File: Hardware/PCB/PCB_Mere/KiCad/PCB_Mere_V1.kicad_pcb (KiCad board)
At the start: 4 copper layers, 73 parts, among them CN1 FTSH-107-01-L-DV-K-A, CN2 B4B-PH-K-S_GNSS, SW1 NRST_BTN, SW2 BOOT_BTN, U1 STM32H723ZGT6, U2 LORA1276-C1-868MHZ, U3 ESP32C3-SUPERMINI, U4 BNO055, U5 B8B-PH-K-S-_TACTIL, U6 B8B-PH-K-S_FILS, U7 B10B-PH-K-S-_SCRN/JOY/ALIM, U8 A-SP1102AR6GHC-A01-2C

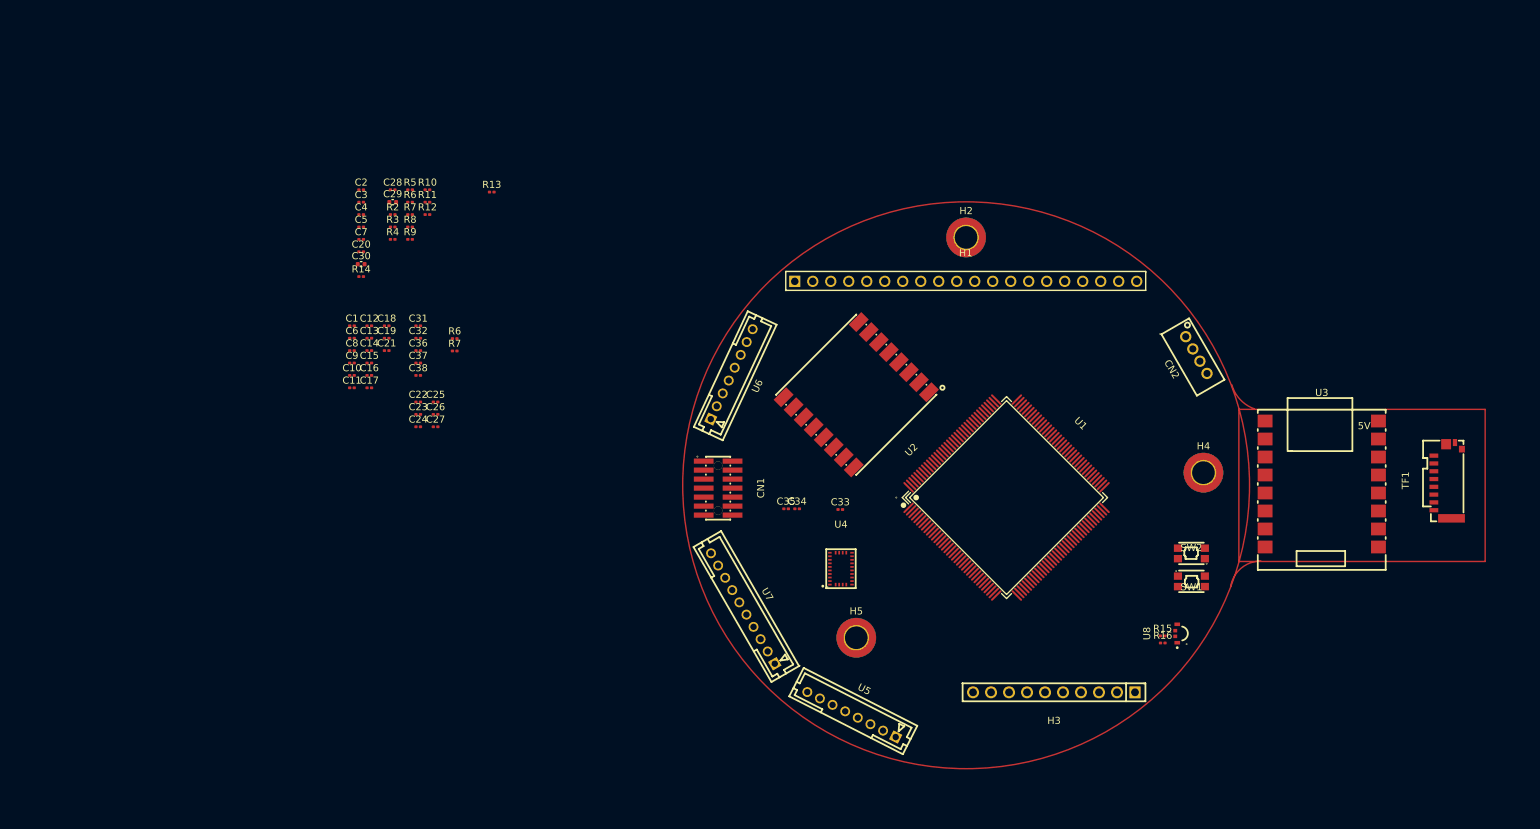
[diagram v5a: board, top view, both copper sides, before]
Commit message: Push PCB_Mère avancement routage
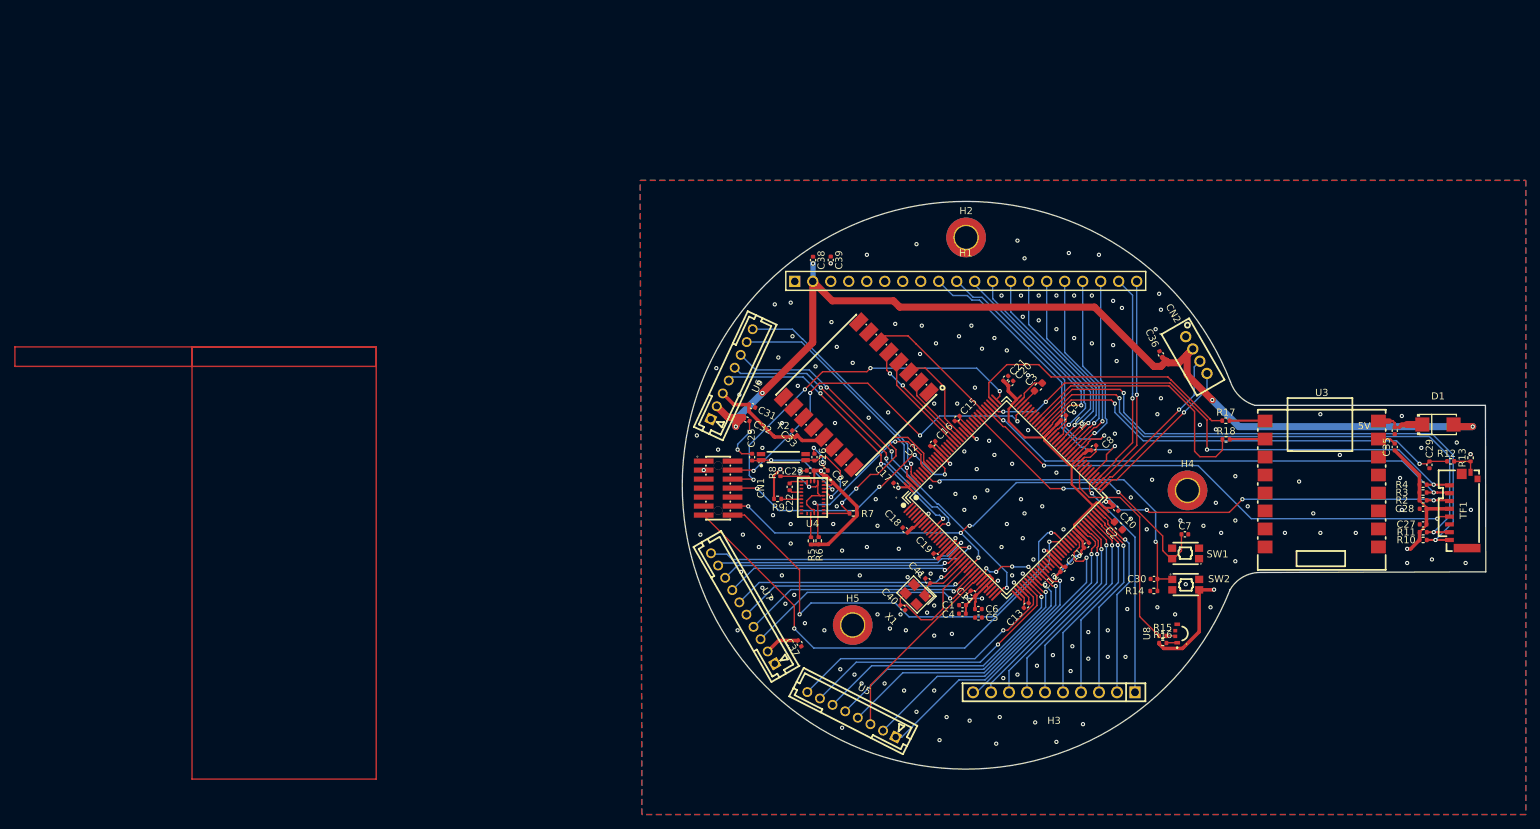
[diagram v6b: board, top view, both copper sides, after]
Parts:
- removed the R6 at (92.0, 53.3)
- removed the R7 at (92.0, 55.1)
- added C39: 100n, Capacitor_SMD:C_0402_1005Metric, F.Cu at (151.4, 61.5)
- added C40: 22p, Capacitor_SMD:C_0402_1005Metric, F.Cu at (161.6, 110.5)
- added C41: 22p, Capacitor_SMD:C_0402_1005Metric, F.Cu at (165.1, 106.8)
- added D1: SS34_C8678, EasyEDA:SMA_L4.3-W2.6-LS5.2-RD, F.Cu at (237.1, 84.7)
- added R17: 1k, Resistor_SMD:R_0402_1005Metric, F.Cu at (207.2, 84.2)
- added R18: 1k, Resistor_SMD:R_0402_1005Metric, F.Cu at (207.2, 86.8)
- added X1: X322525MOB4SI, EasyEDA:CRYSTAL-SMD_4P-L3.2-W2.5-BL, F.Cu at (163.3, 108.7)
- added X2: X701532768KGD4GI, EasyEDA:MC-146_4P-L6.7-W1.5-P0.85-BL, F.Cu at (144.7, 89.3)
- C1, C10, C11, C12, C13, C14, C15, C16, C17, C18, C19, C20, C21, C22, C24, C25, C26, C27, C28, C31, C32, C33, C34, C35, C36, C37, C38, C4, C5, C6, C7, C8, C9: footprint Capacitor_SMD:C_0201_0603Metric -> Capacitor_SMD:C_0402_1005Metric
- C2, C3: footprint Capacitor_SMD:C_0201_0603Metric -> Capacitor_SMD:C_0603_1608Metric
- C23: value 120n -> 100n; footprint Capacitor_SMD:C_0201_0603Metric -> Capacitor_SMD:C_0402_1005Metric
- R10, R11, R12, R13, R14, R15, R16, R2, R3, R4, R5, R6, R7, R8, R9: footprint Resistor_SMD:R_0201_0603Metric -> Resistor_SMD:R_0402_1005Metric
- moved C28 152.2 mm to (235.0, 96.6)
- moved C29 150.9 mm to (235.9, 90.4), turned to -90 degrees
- moved R2 150.9 mm to (235.0, 95.4)
- moved R3 150.2 mm to (235.0, 94.3)
- moved R4 149.5 mm to (235.0, 93.2)
- moved R10 149.0 mm to (235.0, 101.0)
- moved R12 148.6 mm to (238.9, 89.9)
- moved R11 148.1 mm to (235.0, 99.9)
- moved R13 143.1 mm to (241.7, 89.4), turned to 90 degrees
- moved C27 140.1 mm to (235.0, 98.8), turned to 180 degrees
- moved C7 123.5 mm to (201.4, 100.2)
- moved C30 120.4 mm to (197.0, 106.5)
- moved R14 120.4 mm to (197.0, 108.2), turned to 180 degrees
- moved C2 116.9 mm to (192.0, 99.0), turned to 135 degrees
- moved C10 109.4 mm to (191.6, 96.5), turned to -45 degrees
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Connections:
- net TMC2209_AZ_STEP_GPIO_Output renamed TMC2209_AZ_SPREAD_GPIO_Output
- net TMC2209_EL_STEP_GPIO_Output renamed TMC2209_EL_SPREAD_GPIO_Output
- C34 pad 2: +5V -> Net-(D1-K)
- H1 pad 10: unconnected-(H1-Pad10) -> TMC2209_AZ_STDBY_GPIO_Output
- H1 pad 3: unconnected-(H1-Pad3) -> +3.3V
- H1 pad 9: unconnected-(H1-Pad9) -> TMC2209_EL_STDBY_GPIO_Output
- U1 pad 100: unconnected-(U1-PA8-Pad100) -> Net-(U1-PA8)
- U1 pad 110: unconnected-(U1-PA15-Pad110) -> Net-(U1-PA15)
- U1 pad 114: unconnected-(U1-PD0-Pad114) -> LoRa_NRST_STM_GPIO_Output
- U1 pad 23: unconnected-(U1-PH0-OSC_IN-Pad23) -> /OSC_IN
- U1 pad 24: unconnected-(U1-PH1-OSC_OUT-Pad24) -> /OSC_OUT
- U1 pad 58: ESP32_UART7_RX -> unconnected-(U1-PE7-Pad58)
- U1 pad 59: ESP32_UART7_TX -> unconnected-(U1-PE8-Pad59)
- U1 pad 78: unconnected-(U1-PD9-Pad78) -> TMC2209_EL_STDBY_GPIO_Output
- U1 pad 85: unconnected-(U1-PD14-Pad85) -> TMC2209_AZ_STDBY_GPIO_Output
- U2 pad 6: unconnected-(U2-NRESET-Pad6) -> LoRa_NRST_STM_GPIO_Output
- U3 pad 14: +3.3V -> unconnected-(U3-3V3-Pad14)
- U3 pad 16: +5V -> Net-(D1-K)
- U4 pad 28: unconnected-(U4-VDDIO-Pad28) -> +3.3V
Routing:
- net +3.3V: track 0.00 -> 168.9 mm, vias 0 -> 16
- net +5V: track 0.00 -> 144.3 mm, vias 0 -> 5
- net NRST_STM: track 0.00 -> 82.9 mm, vias 0 -> 5
- net SD_D1: track 0.00 -> 82.0 mm, vias 0 -> 2
- net SD_D0: track 0.00 -> 78.9 mm, vias 0 -> 2
- net SD_D2: track 0.00 -> 76.2 mm, vias 0 -> 4
- net SD_CMD: track 0.00 -> 73.9 mm, vias 0 -> 4
- net SD_CK: track 0.00 -> 71.9 mm, vias 0 -> 2
- net SD_D3: track 0.00 -> 71.1 mm, vias 0 -> 2
- net GND: track 0.00 -> 69.2 mm, vias 0 -> 191
- net JTAG_UART9_RX: track 0.00 -> 68.9 mm, vias 0 -> 2
- net JTAG_UART9_TX: track 0.00 -> 66.1 mm, vias 0 -> 2
- net SD_DETECT: track 0.00 -> 63.1 mm, vias 0 -> 2
- net ID-EXT_ADC1_INP14: track 0.00 -> 55.0 mm, vias 0 -> 3
- net DEBUG_JTMS-SWDIO: track 0.00 -> 54.3 mm, vias 0 -> 4
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- added copper zone on In2.Cu, net +3.3V
- added copper zone on B.Cu, net GND
- added copper zone on F.Cu, net GND
- added copper zone on In1.Cu, net GND
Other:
- board outline added: 113.4 x 80.1 mm
- rule pad_to_mask_clearance: 0 -> 0.1

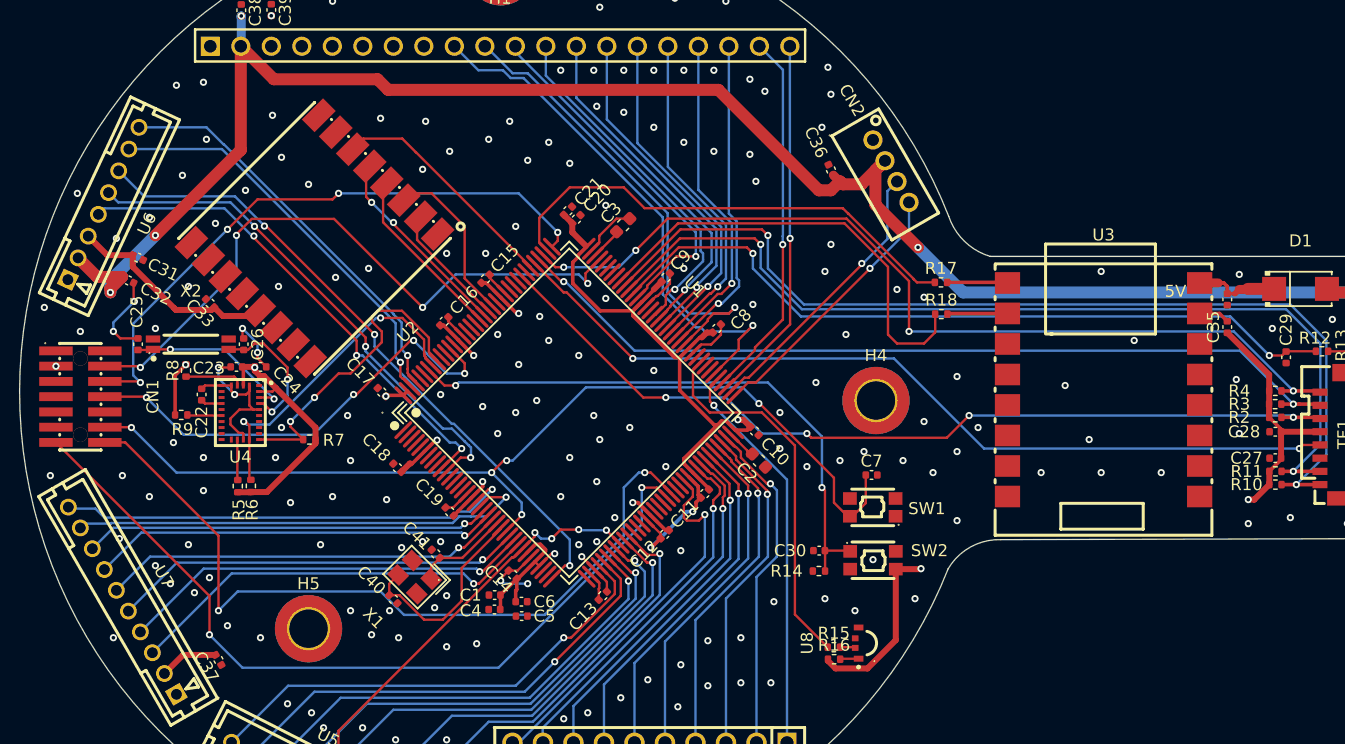
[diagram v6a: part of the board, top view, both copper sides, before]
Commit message: Push PCB_Mère avancement routage
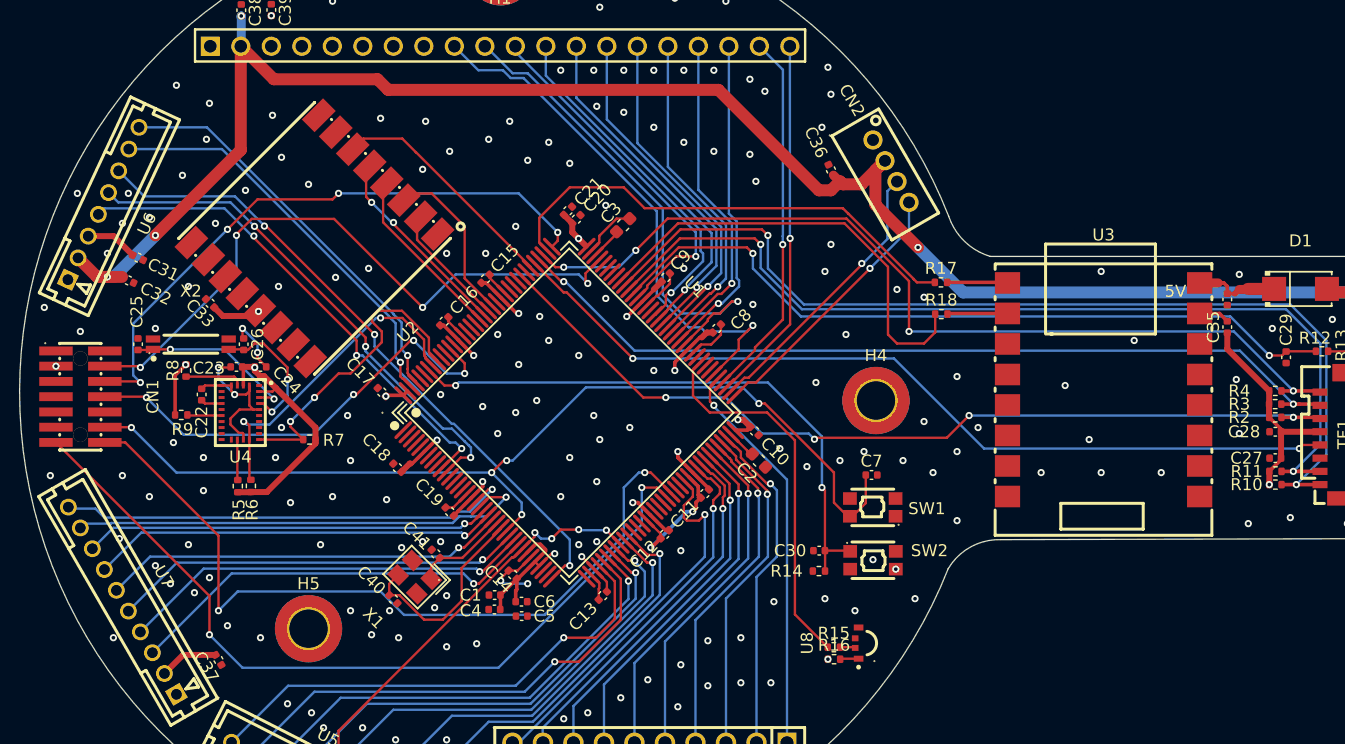
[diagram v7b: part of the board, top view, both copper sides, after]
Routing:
- net +3.3V: track 168.9 -> 115.0 mm, vias 16 -> 22
- net GND: track 69.2 -> 62.1 mm, vias 191 -> 188
- net +5V: track 144.3 -> 141.8 mm
- net TMC2209_AZ_STDBY_GPIO_Output: track 39.7 -> 40.9 mm
- net TACTIL_SPI6_NSS: track 39.9 -> 41.1 mm
- net TACTIL_SPI6_SCK: track 39.5 -> 40.6 mm

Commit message: Finalisation de la PCB_Mere, need vérification
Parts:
- moved C41 1.03 mm to (166.0, 107.2)
- moved R16 1.02 mm to (199.0, 116.2), turned to 90 degrees
- moved C34 0.75 mm to (231.8, 85.6)
- moved C35 0.75 mm to (231.8, 87.9)
- moved R15 0.33 mm to (198.5, 114.8)
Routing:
- net +5V: track 141.8 -> 12.0 mm, vias 5 -> 2
- net +3.3V: track 115.0 -> 109.6 mm, vias 22 -> 27
- net GND: track 62.1 -> 59.8 mm, vias 188 -> 193
- net LoRa_SPI1_MISO: track 10.4 -> 11.5 mm
- net LoRa_SPI1_MOSI: track 14.0 -> 14.9 mm
- net LoRa_SPI1_NSS: track 16.6 -> 17.5 mm
- net /OSC_IN: track 7.99 -> 7.37 mm
- net LoRa_SPI1_SCK: track 14.8 -> 15.3 mm
- added copper zone on In2.Cu, net +5V
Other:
- rule pad_to_mask_clearance: 0.1 -> 0
